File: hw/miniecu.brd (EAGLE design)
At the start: 50 x 50 mm, 65 parts

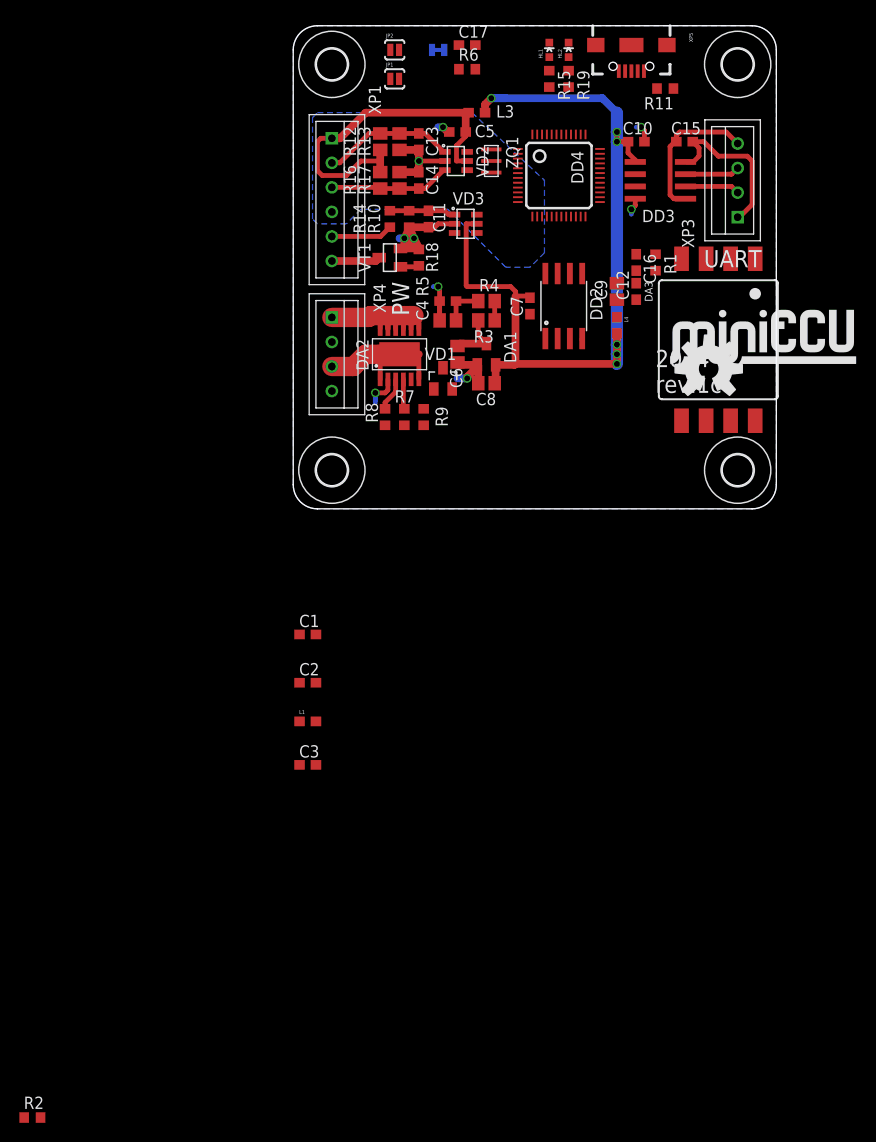
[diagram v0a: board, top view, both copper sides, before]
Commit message: hw: add SWD, EXT connectors; sch done
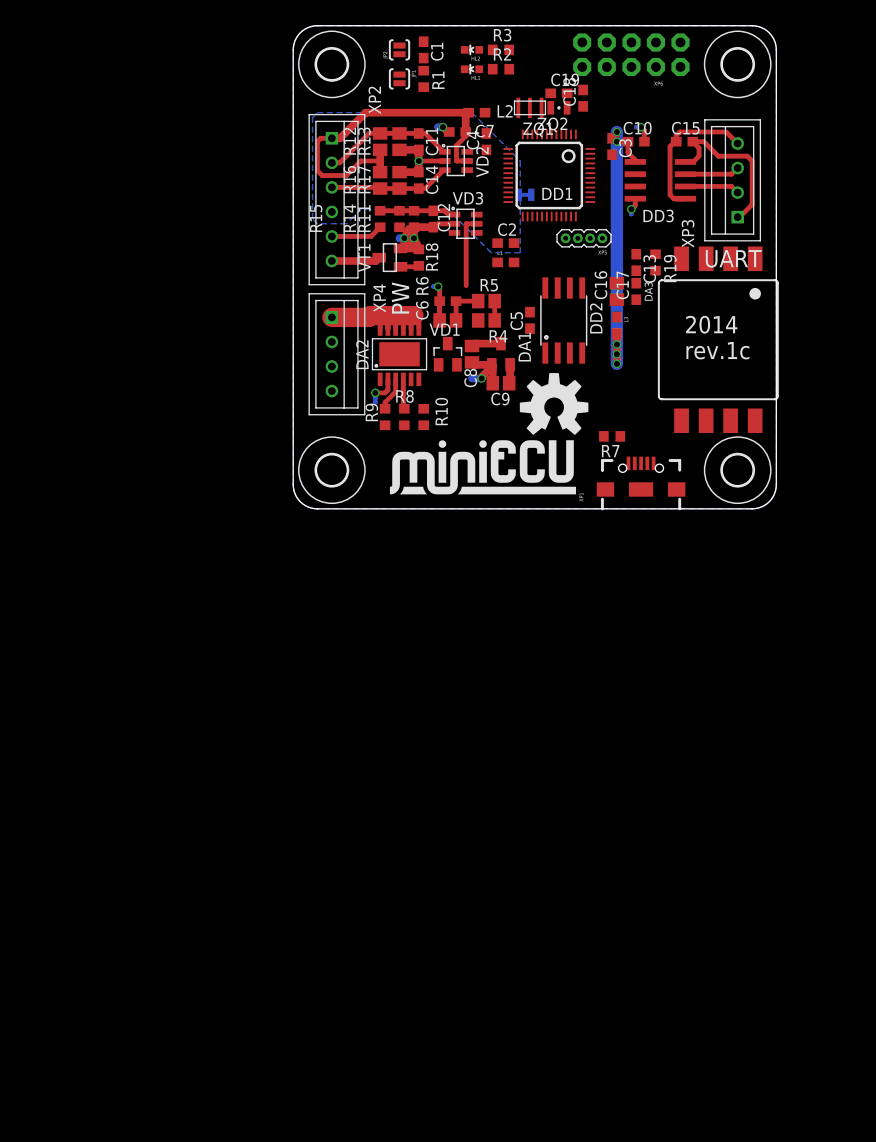
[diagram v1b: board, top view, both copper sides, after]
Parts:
- removed DD4: STM32F373C, stm32f373:LQFP48
- removed L4: FB, SparkFun-Passives:0603
- added C18, C19: 10p, resistor:C0603
- added DD1: STM32F373C, stm32f373:LQFP48
- added L2: FB, SparkFun-Passives:0603
- added XP2: B6B-XH-A, miniecu-con:B6B-XH
- added XP6: M05X2NO_SILK, SparkFun-Connectors:2X5_NOSILK
- added ZQ2: FC-12M, crystal:FC-12M
- C11: value 0.022 -> 0.1
- C12: value 0.01 -> 22p
- C13: value 0.1 -> 0.33
- C16: value 0.33 -> 1.0; device resistor:C0603 -> resistor:C0805
- C17: value 0.1 -> 0.01
- C6: value 1.0 -> 0.1; device resistor:C0805 -> resistor:C0603
- LOGO1: value OSHW-LOGOL -> MINIECU_LOGO; device SparkFun-Aesthetics:OSHW-LOGO-L -> miniecu:MINIECU_LOGO
- LOGO2: value MINIECU_LOGO -> OSHW-LOGOL; device miniecu:MINIECU_LOGO -> SparkFun-Aesthetics:OSHW-LOGO-L
- R1: value 750 -> 10k
- R11: value 1.5k -> 10k
- R15: value 140 -> 10k
- R19: value 140 -> 750
- R2, R9: value 10k -> 140
- R3: value 10k 1% -> 140; device resistor:R0805 -> resistor:R0603
- R6: value 10k -> 10k 1%; device resistor:R0603 -> resistor:R0805
- R7: value 1k -> 1.5k
- R8: value 140 -> 1k
- XP1: value B6B-XH-A -> USB_MICROB_PLUGCONN-11752; device miniecu-con:B6B-XH -> SparkFun-Connectors:USB-B-MICRO-SMD_V03
- XP5: value USB_MICROB_PLUGCONN-11752 -> SWD; device SparkFun-Connectors:USB-B-MICRO-SMD_V03 -> miniecu-con:1X04-1.27MM
- moved R2 118.8 mm to (21.5, 45.5)
- moved C3 71.3 mm to (33.0, 37.5), turned to 270 degrees
- moved C1 61.7 mm to (13.5, 47.5), turned to 270 degrees
- moved L1 51.7 mm to (22.0, 25.5)
- moved C2 49.9 mm to (22.0, 27.5)
- moved XP1 43.9 mm to (36.0, 2.00), turned to 90 degrees
- moved LOGO1 35.5 mm to (10.0, 1.50)
- moved C17 30.9 mm to (35.5, 22.5), turned to 90 degrees
- moved R1 30.6 mm to (13.5, 44.5)
- moved R11 29.3 mm to (12.5, 30.0), turned to 90 degrees
- moved R3 28.0 mm to (21.5, 47.5), turned to 0 degrees
- moved L3 26.3 mm to (33.5, 19.0), turned to 270 degrees
- moved R6 26.1 mm to (16.0, 19.5)
- moved C13 25.7 mm to (35.5, 25.5)
- moved R15 22.7 mm to (9.00, 30.0)
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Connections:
- net VBAT renamed V_BAT
- removed net BAT: DD4.1
- removed net N$10: C17.1, DD4.7, JP2.2
- removed net N$11: DD4.44, JP1.1, R6.2
- removed net N$3: C12.1, C9.1, DA3.2, L4.1
- removed net N$5: C2.1, DD4.24, DD4.25, DD4.9, L1.1
- removed net OSC32I: DD4.3
- removed net OSC32O: DD4.4
- new net !NRST: C1.1, DD1.7, JP2.2
- new net AVCC: C2.1, DD1.24, DD1.25, DD1.9, L1.1
- new net AVCC_FLOW: C16.1, C17.1, DA3.2, L3.1
- new net BOOT0: DD1.44, JP1.1, R1.2
- new net CAN_RX: DD1.45, XP6.7
- new net CAN_TX: DD1.46, XP6.8
- new net PA1: DD1.11, XP6.5
- new net PA2: DD1.12, XP6.6
- new net PC13: DD1.2, XP6.4
- new net RTCBAT: DD1.1, XP6.3
- new net RTCIN: C18.1, DD1.3, ZQ2.1
- new net RTCOUT: C19.1, DD1.4, ZQ2.2
- new net SCL: DD1.42, XP6.9
- new net SDA: DD1.43, XP6.10
- net +3V3: now also C4.1, C5.1, C9.1, DD1.17, DD1.48, L2.2, R7.2, XP5.1, XP6.1; no longer C1.1, C7.1, C8.1, DD4.17, DD4.48, JP1.2, L4.2, R11.2
- net AGND: now also C11.2, C7.2, DD1.23, DD1.8, XP2.4; no longer C13.2, C5.2, DD4.23, DD4.8, XP1.4
- net AVCC_EXT: now also C7.1, JP1.2, L2.1, XP2.1; no longer C5.1, L3.1, XP1.1
- net FLASH_CS: now also DD1.26
- net FLOW: now also C13.1, DD1.28, R19.1; no longer C16.1, DD4.21, R1.1
- net GND: now also C13.2, C18.2, C19.2, C5.2, DD1.47, R1.1, R11.1, R14.1, R8.2, XP1.GND1, XP5.3, XP6.2; no longer C11.2, C7.2, DD4.47, R2.1, R5.1, R7.2, R9.1, XP5.GND1
- net IGN_EN: now also DD1.22, R9.1; no longer R8.1
- net LED_G: now also DD1.14, R2.2; no longer R15.2
- net LED_R: now also DD1.13, R3.2; no longer R19.2
- net MISO: now also DD1.40
- net MOSI: now also DD1.41
- net N$1: now also R4.1, R5.2; no longer R3.1, R4.2
- net N$12: now also R3.1; no longer R19.1
- net N$2: now also R8.1; no longer R7.1
- net N$4: now also R19.2; no longer R1.2
- net N$6: now also C8.1, R4.2; no longer C6.1, R3.2
- net N$7: now also R9.2; no longer R8.2
- net N$8: now also R2.1; no longer R15.1
- net N$9: now also R10.2; no longer R9.2
- net OIL_PRES: now also DD1.19, XP2.3; no longer DD4.19, XP1.3
- net OSC_IN: now also DD1.5; no longer DD4.5
- net OSC_OUT: now also DD1.6; no longer DD4.6
- net RPM_IN: now also C12.1, DD1.10, R11.2, R14.2, R15.1; no longer C11.1, DD4.10, R10.2, R14.1, R2.2
- net RPM_IN_CON: now also R15.2, XP2.5; no longer R14.2, XP1.5
- net RXD: now also DD1.31; no longer DD4.31
- net SCK: now also DD1.39
- net STARTER: now also DD1.21
- net STARTER_OUT: now also XP2.6; no longer XP1.6
- net SWCLK: now also DD1.37, XP5.2; no longer DD4.37
- net SWDIO: now also DD1.34, XP5.4; no longer DD4.34
- net THERM: now also C11.1, DD1.18, XP2.2; no longer C13.1, DD4.18, XP1.2
- net TXD: now also DD1.30; no longer DD4.30
- net USB_DM: now also DD1.32, XP1.D-1; no longer DD4.32, XP5.D-1
- net USB_DP: now also DD1.33, R7.1, XP1.D+1; no longer DD4.33, R11.1, XP5.D+1
- net USB_VBUS: now also XP1.VBUS1; no longer XP5.VBUS1
- net V_SENSE: now also C6.1, DD1.20, R5.1, R6.2; no longer C4.1, DD4.20, R4.1, R5.2
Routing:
- net +3V3: track 87.2 -> 40.5 mm, vias 6 -> 5
- net V_BAT: track 14.7 -> 0.00 mm
- net N$6: track 5.86 -> 3.10 mm
- net RPM_IN_CON: track 6.40 -> 5.40 mm
- net RPM_IN: track 6.87 -> 7.87 mm

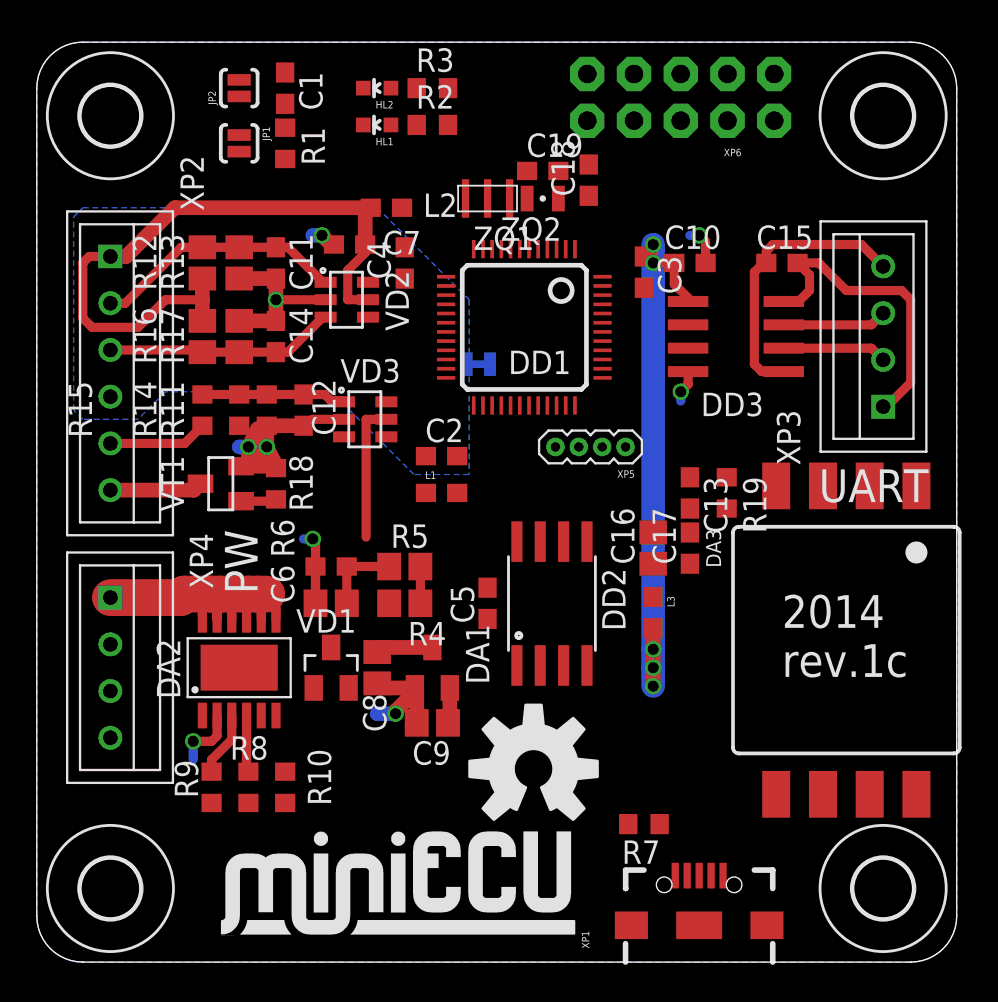
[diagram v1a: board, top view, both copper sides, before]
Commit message: hw: route top half
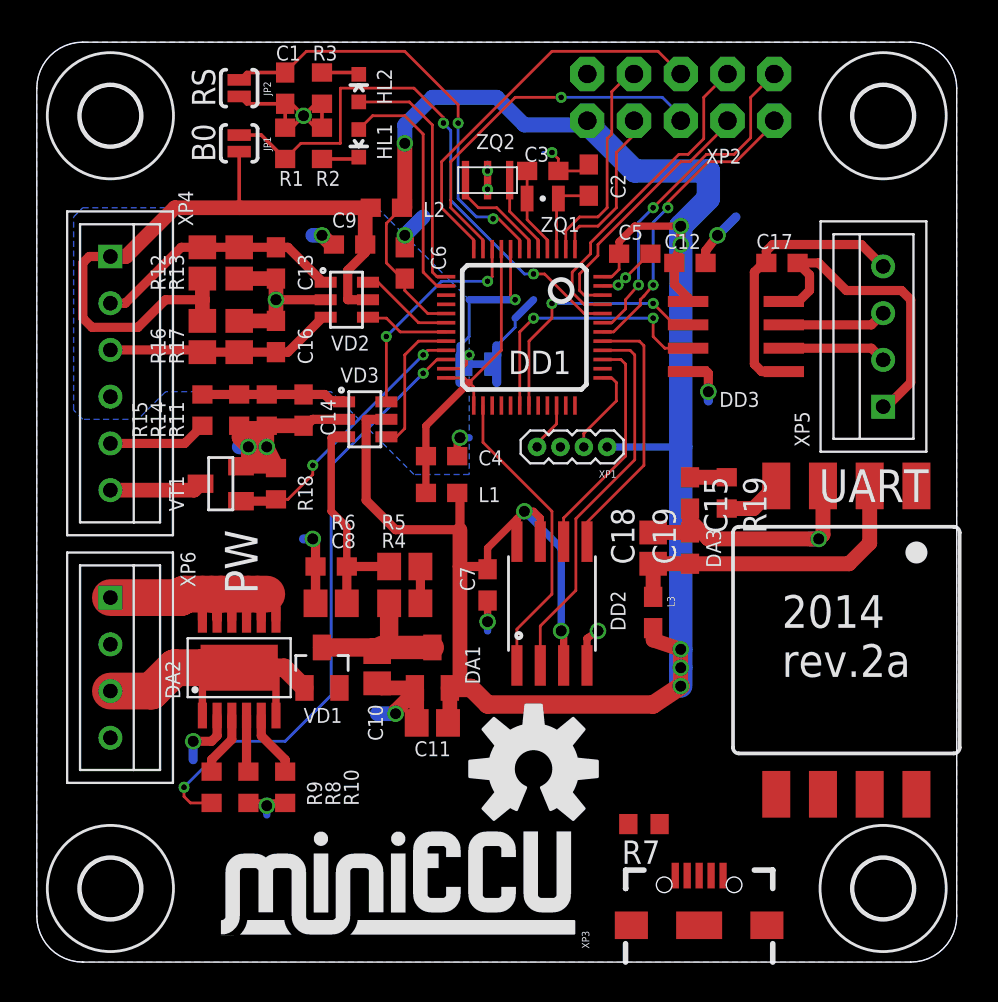
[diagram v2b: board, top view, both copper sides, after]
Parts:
- C10, C11: value 0.1 -> 1.0; device resistor:C0603 -> resistor:C0805
- C12: value 22p -> 0.1
- C13: value 0.33 -> 0.1
- C14: value 0.1 -> 22p
- C15: value 0.1 -> 0.33
- C16, C8, C9: value 1.0 -> 0.1; device resistor:C0805 -> resistor:C0603
- C17: value 0.01 -> 0.1
- C18: value 10p -> 1.0; device resistor:C0603 -> resistor:C0805
- C19: value 10p -> 0.01
- C2, C3: value 0.1 -> 10p
- XP1: value USB_MICROB_PLUGCONN-11752 -> SWD; device SparkFun-Connectors:USB-B-MICRO-SMD_V03 -> miniecu-con:1X04-1.27MM
- XP2: value B6B-XH-A -> M05X2NO_SILK; device miniecu-con:B6B-XH -> SparkFun-Connectors:2X5_NOSILK
- XP3: value B4B-XH-A -> USB_MICROB_PLUGCONN-11752; device miniecu-con:B4B-XH -> SparkFun-Connectors:USB-B-MICRO-SMD_V03
- XP4: value B4B-XH-A -> B6B-XH-A; device miniecu-con:B4B-XH -> miniecu-con:B6B-XH
- XP5: value SWD -> B4B-XH-A; device miniecu-con:1X04-1.27MM -> miniecu-con:B4B-XH
- XP6: value M05X2NO_SILK -> B4B-XH-A; device SparkFun-Connectors:2X5_NOSILK -> miniecu-con:B4B-XH
- ZQ1: value CSTCE8M00G52-R0 -> FC-12M; device cstce-resonator:CSTCE -> crystal:FC-12M
- ZQ2: value FC-12M -> CSTCE8M00G52-R0; device crystal:FC-12M -> cstce-resonator:CSTCE
- moved XP6 43.8 mm to (4.00, 16.0), turned to 270 degrees
- moved XP2 34.4 mm to (35.0, 47.0), turned to 90 degrees
- moved XP3 33.5 mm to (36.0, 2.00)
- moved C10 27.8 mm to (18.5, 16.0), turned to 270 degrees
- moved XP1 26.5 mm to (31.0, 28.0), turned to 180 degrees
- moved C11 26.4 mm to (21.5, 13.0), turned to 180 degrees
- moved C9 26.4 mm to (17.0, 39.0)
- moved C13 25.7 mm to (13.0, 38.0)
- moved C16 23.5 mm to (13.0, 34.0)
- moved C12 22.5 mm to (35.5, 38.0), turned to 0 degrees
- moved C19 22.0 mm to (35.5, 22.5), turned to 90 degrees
- moved C5 20.6 mm to (32.5, 38.5), turned to 0 degrees
- moved C18 20.3 mm to (33.5, 22.5)
- moved C7 20.0 mm to (24.5, 20.5), turned to 270 degrees
- moved C2 17.0 mm to (30.0, 42.5), turned to 90 degrees
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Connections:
- removed net N$12: HL2.A, R3.1
- removed net N$8: HL1.A, R2.1
- new net N$3: HL2.C, R3.2
- new net N$5: HL1.C, R2.2
- net +3V3: now also C11.1, C12.1, C6.1, C7.1, XP1.1, XP2.1; no longer C10.1, C3.1, C4.1, C9.1, XP5.1, XP6.1
- net AGND: now also C13.2, C16.2, C4.2, C9.2, XP4.4; no longer C11.2, C14.2, C2.2, C7.2, XP2.4
- net AVCC: now also C4.1; no longer C2.1
- net AVCC_EXT: now also C9.1, XP4.1; no longer C7.1, XP2.1
- net AVCC_FLOW: now also C18.1, C19.1; no longer C16.1, C17.1
- net CAN_RX: now also XP2.8; no longer XP6.7
- net CAN_TX: now also XP2.7; no longer XP6.8
- net FLOW: now also C15.1; no longer C13.1
- net GND: now also C11.2, C14.2, C15.2, C2.2, C7.2, R2.1, R3.1, XP1.3, XP2.2, XP3.GND1, XP6.4, ZQ2.2; no longer C13.2, C16.2, C17.2, C4.2, C9.2, HL1.C, HL2.C, XP1.GND1, XP4.2, XP4.4, XP5.3, ZQ1.2
- net GND2: now also C17.2, XP5.4; no longer C15.2, XP3.4
- net IORXD: now also XP5.3; no longer XP3.3
- net IOTXD: now also XP5.2; no longer XP3.2
- net LED_G: now also HL1.A; no longer R2.2
- net LED_R: now also HL2.A; no longer R3.2
- net N$6: now also C10.1; no longer C8.1
- net OIL_PRES: now also C16.1, XP4.3; no longer C14.1, XP2.3
- net OSC_IN: now also ZQ2.1; no longer ZQ1.1
- net OSC_OUT: now also ZQ2.3; no longer ZQ1.3
- net PA1: now also XP2.5; no longer XP6.5
- net PA2: now also XP2.6; no longer XP6.6
- net PC13: now also XP2.4; no longer XP6.4
- net RPM_IN: now also C14.1; no longer C12.1
- net RPM_IN_CON: now also XP4.5; no longer XP2.5
- net RTCBAT: now also XP2.3; no longer XP6.3
- net RTCIN: now also C2.1, ZQ1.1; no longer C18.1, ZQ2.1
- net RTCOUT: now also C3.1, ZQ1.2; no longer C19.1, ZQ2.2
- net SCL: now also XP2.9; no longer XP6.9
- net SDA: now also XP2.10; no longer XP6.10
- net STARTER_OUT: now also XP4.6; no longer XP2.6
- net SWCLK: now also XP1.2; no longer XP5.2
- net SWDIO: now also XP1.4; no longer XP5.4
- net THERM: now also C13.1, XP4.2; no longer C11.1, XP2.2
- net USB_DM: now also XP3.D-1; no longer XP1.D-1
- net USB_DP: now also XP3.D+1; no longer XP1.D+1
- net USB_VBUS: now also XP3.VBUS1; no longer XP1.VBUS1
- net VCC2: now also C17.1, XP5.1; no longer C15.1, XP3.1
- net V_BAT: now also XP6.3; no longer XP4.3
- net V_IGN: now also XP6.1; no longer XP4.1
- net V_SENSE: now also C8.1; no longer C6.1
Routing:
- net +3V3: track 40.5 -> 134.8 mm, vias 5 -> 8
- net GND: track 36.3 -> 87.1 mm, vias 7 -> 18
- net IGN_EN: track 0.00 -> 33.3 mm, vias 0 -> 2
- net BOOT0: track 0.00 -> 31.1 mm, vias 0 -> 2
- net !NRST: track 0.00 -> 24.0 mm, vias 0 -> 2
- net PA2: track 0.00 -> 21.5 mm
- net MISO: track 0.00 -> 20.9 mm
- net PA1: track 0.00 -> 20.1 mm, vias 0 -> 1
- net SDA: track 0.00 -> 18.5 mm, vias 0 -> 2
- net AVCC: track 0.00 -> 17.7 mm
- net CAN_RX: track 0.00 -> 17.6 mm
- net AVCC_FLOW: track 0.00 -> 17.1 mm
- net V_BAT: track 0.00 -> 16.7 mm
- net SCL: track 0.00 -> 16.5 mm, vias 0 -> 2
- net FLASH_CS: track 0.00 -> 16.5 mm
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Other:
- board text added: "2014 rev.2a"
- board text added: "B0"
- board text added: "RS"
- board text added: "miniECU rev.2a engine monitoring with kill switch"
- board text removed: "2014 rev.1c"
- board text removed: "miniECU rev.1c engine monitoring with kill switch"

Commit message: hw: hw_2.0a routed
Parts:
- moved R7 4.03 mm to (37.0, 7.00), turned to 0 degrees
- moved LOGO2 1.12 mm to (28.0, 11.0)
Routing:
- net USB_DP: track 0.00 -> 34.4 mm, vias 0 -> 2
- net USB_DM: track 0.00 -> 33.7 mm, vias 0 -> 2
- net USB_VBUS: track 0.00 -> 25.1 mm
- net FLOW: track 2.00 -> 15.0 mm, vias 0 -> 2
- net +3V3: track 134.8 -> 143.9 mm, vias 8 -> 9
- net GND: track 87.1 -> 93.1 mm, vias 18 -> 19
- net N$8: track 1.00 -> 0.00 mm
- net AGND: track 25.4 -> 25.9 mm

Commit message: hw: release hw_2.0a
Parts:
- C2, C3: value 10p -> 6p
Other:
- board text added: "EXT"
- board text added: "SWD"
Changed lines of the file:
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@@
 <text x="9.7" y="43.5" size="1.27" layer="121" font="vector" rot="R90">B0</text>
 <text x="9.7" y="46.5" size="1.27" layer="121" font="vector" rot="R90">RS</text>
+<text x="26.5" y="50" size="1.778" layer="112" font="vector" rot="R270">EXT</text>
+<text x="26.5" y="25" size="1.9304" layer="21" font="vector">SWD</text>
 </plain>
 <attributes>
@@
 <element name="LOGO1" library="miniecu" package="MINIECU_LOGO" value="MINIECU_LOGO" x="10" y="1.5"/>
 <element name="DD1" library="stm32f373" package="LQFP48" value="STM32F373C" x="26.5" y="34.5" smashed="yes" rot="R180">
-<attribute name="NAME" x="29.04" y="33.23" size="0.8128" layer="25" font="vector" rot="R180"/>
+<attribute name="NAME" x="23.04" y="31.23" size="0.8128" layer="25" font="vector" rot="R180"/>
 <attribute name="VALUE" x="29.04" y="35.77" size="1.27" layer="27" rot="R180"/>
 </element>
@@
 <element name="XP3" library="SparkFun-Connectors" package="USB-B-MICRO-SMD_V03" value="USB_MICROB_PLUGCONN-11752" x="36" y="2" smashed="yes" rot="R90">
 <attribute name="PROD_ID" value="CONN-11752" x="36" y="2" size="1.778" layer="27" rot="R90" display="off"/>
-<attribute name="NAME" x="30.031" y="0.73" size="0.8128" layer="25" font="vector" rot="R90"/>
+<attribute name="NAME" x="31.031" y="3.23" size="0.8128" layer="25" font="vector" rot="R90"/>
 <attribute name="VALUE" x="30.539" y="0.73" size="0.4064" layer="27" rot="R90"/>
 </element>
@@
 <attribute name="VALUE" x="17.532" y="46.611" size="1.27" layer="27" rot="R90"/>
 </element>
-<element name="XP1" library="miniecu-con" package="1X04-1.27MM" value="SWD" x="31" y="28" rot="R180"/>
+<element name="XP1" library="miniecu-con" package="1X04-1.27MM" value="SWD" x="31" y="28" smashed="yes" rot="R180">
+<attribute name="NAME" x="32" y="30" size="0.8128" layer="25" font="vector" rot="R180"/>
+<attribute name="VALUE" x="31.508" y="29.651" size="0.4064" layer="27" rot="R180"/>
+</element>
 <element name="ZQ1" library="crystal" package="FC-12M" value="FC-12M" x="27.5" y="41.5" smashed="yes" rot="R180">
 <attribute name="NAME" x="29.5" y="40.5" size="0.8128" layer="25" font="vector" rot="R180"/>
 <attribute name="VALUE" x="28.525" y="43.65" size="1.27" layer="27" rot="R180"/>
 </element>
-<element name="C2" library="resistor" package="C0603" value="10p" x="30" y="42.5" smashed="yes" rot="R90">
+<element name="C2" library="resistor" package="C0603" value="6p" x="30" y="42.5" smashed="yes" rot="R90">
 <attribute name="NAME" x="32" y="41.5" size="0.8128" layer="25" font="vector" rot="R90"/>
 <attribute name="VALUE" x="32.032" y="41.611" size="1.27" layer="27" rot="R90"/>
 </element>
-<element name="C3" library="resistor" package="C0603" value="10p" x="27.5" y="43" smashed="yes">
+<element name="C3" library="resistor" package="C0603" value="6p" x="27.5" y="43" smashed="yes">
 <attribute name="NAME" x="26.5" y="43.5" size="0.8128" layer="25" font="vector"/>
 <attribute name="VALUE" x="26.611" y="40.968" size="1.27" layer="27"/>
